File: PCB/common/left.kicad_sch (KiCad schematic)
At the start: 89 parts, among them J2 TRS

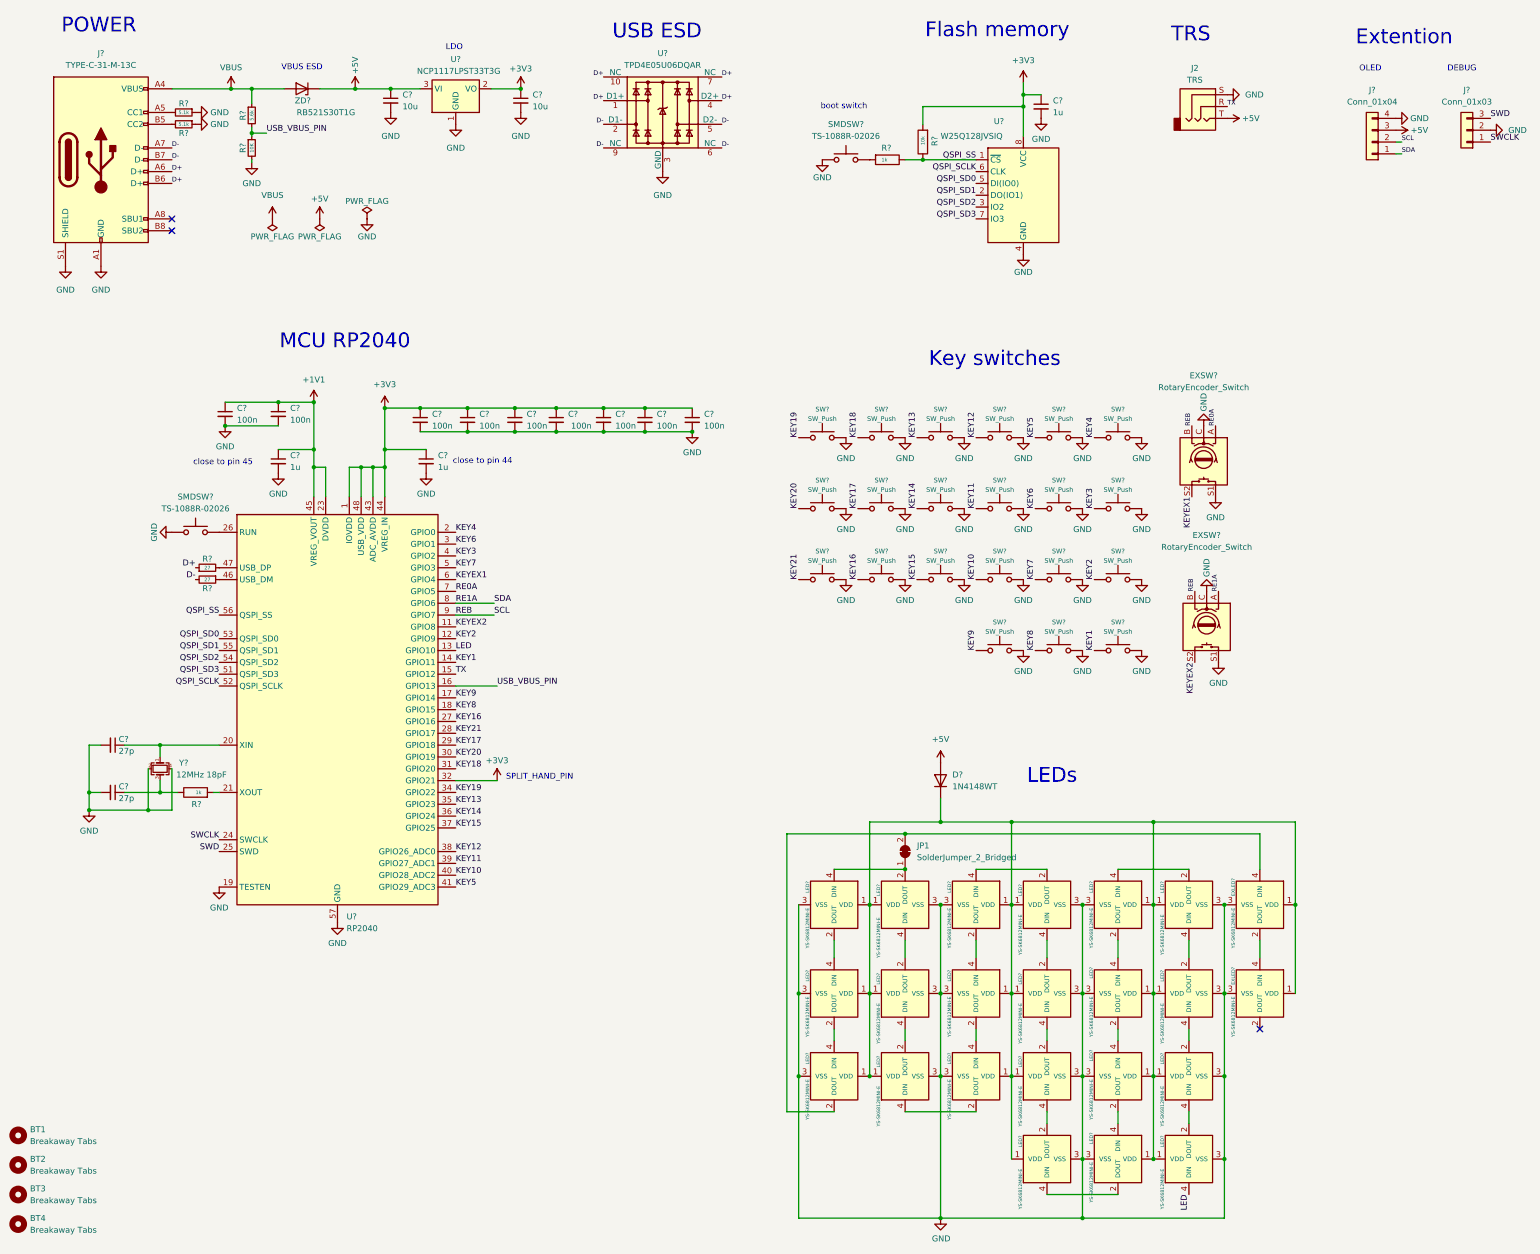
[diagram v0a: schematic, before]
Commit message: Removed unused electronics
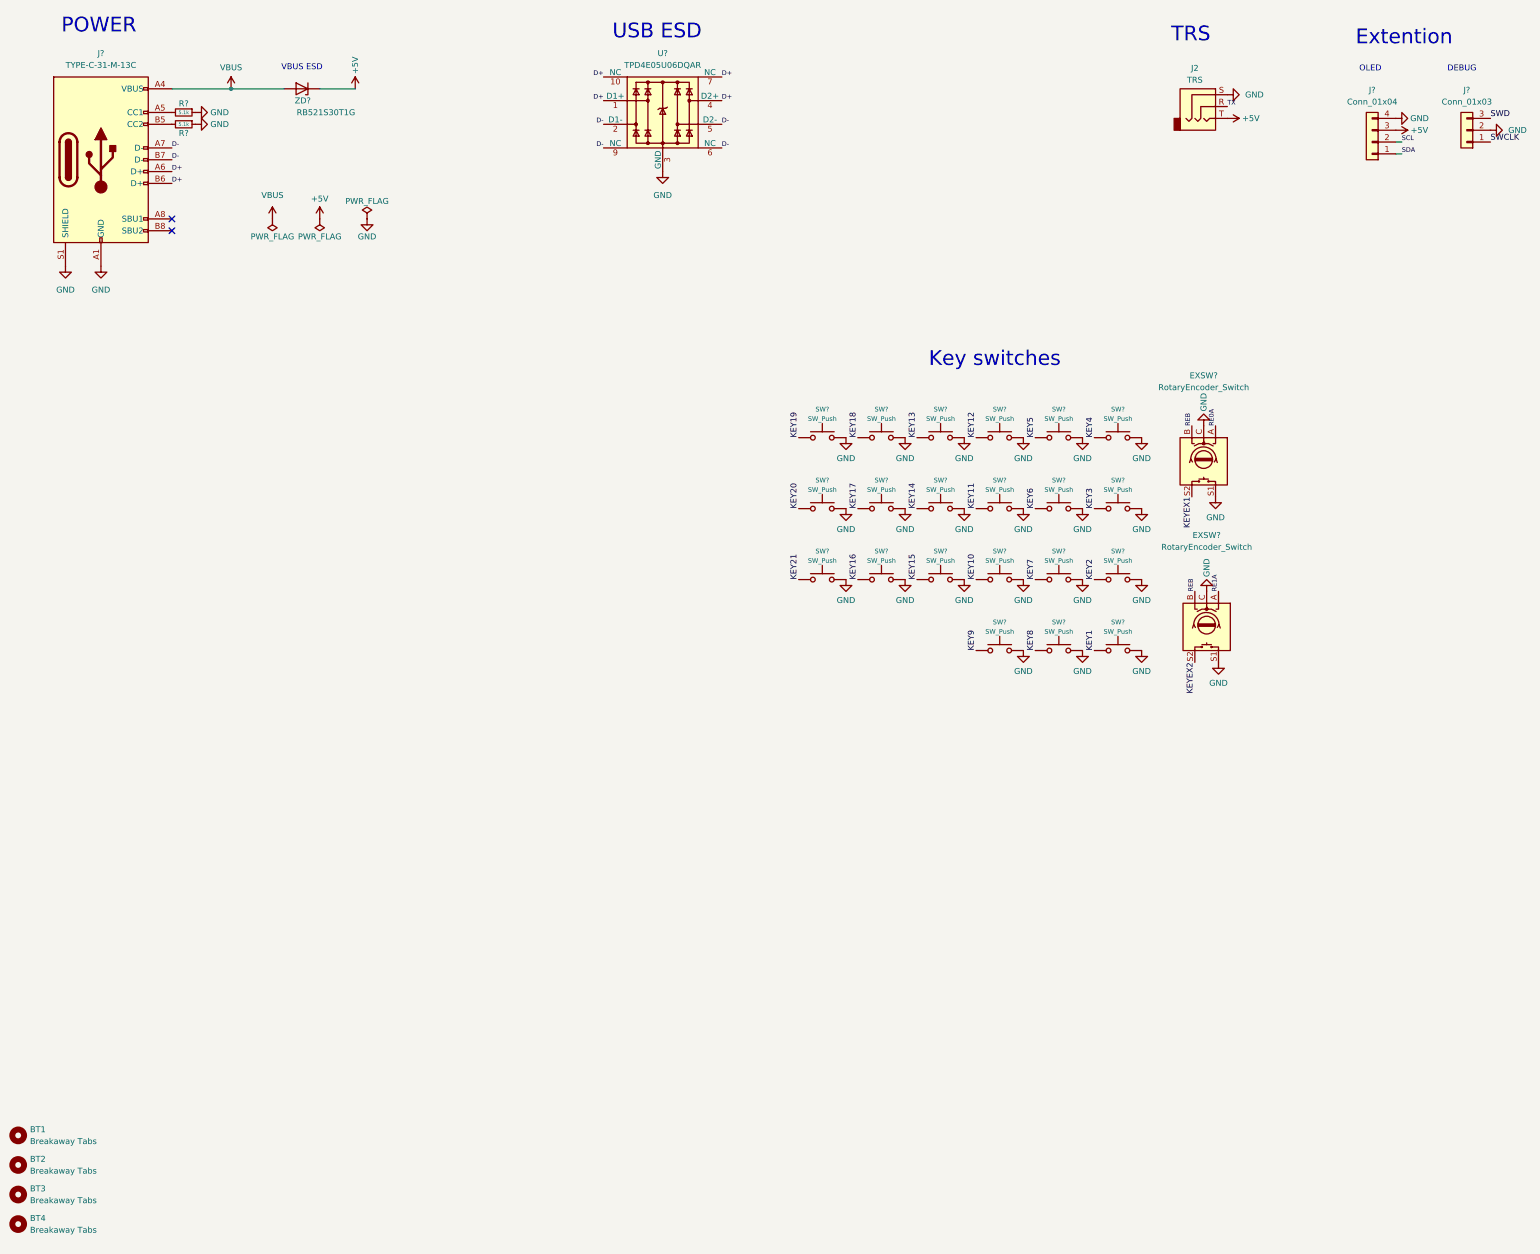
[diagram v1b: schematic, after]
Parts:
- removed C? (x2): 27p, Capacitor_SMD:C_0402_1005Metric, symbol Device:C_Small
- removed C? (x9): 100n, Capacitor_SMD:C_0402_1005Metric, symbol Device:C_Small
- removed C? (x3): 1u, Capacitor_SMD:C_0402_1005Metric, symbol Device:C_Small
- removed C? (x2): 10u, Capacitor_SMD:C_0402_1005Metric, symbol Device:C_Small
- removed D?: 1N4148WT, Diode_SMD:D_SOD-523, symbol Diode:1N4148WT
- removed EXLED? (x2), LED? (x21): YS-SK6812MINI-E, kbd_local:YS-SK6812MINI-E, symbol kbd_local:YS-SK6812MINI-E
- removed JP1: SolderJumper_2_Bridged, Jumper:SolderJumper-2_P1.3mm_Open_RoundedPad1.0x1.5mm, symbol Jumper:SolderJumper_2_Bridged
- removed R? (x2): 27, Resistor_SMD:R_0402_1005Metric, symbol Device:R_Small
- removed R?: 10K, Resistor_SMD:R_0402_1005Metric, symbol Device:R_Small
- removed R?: 5.6k, Resistor_SMD:R_0402_1005Metric, symbol Device:R_Small
- removed R?: 10k, Resistor_SMD:R_0402_1005Metric, symbol Device:R
- removed R? (x2): 1k, Resistor_SMD:R_0402_1005Metric, symbol Device:R
- removed SMDSW? (x2): TS-1088R-02026, kbd_local:TS-1088R-02026, symbol Switch:SW_Push
- removed U?: RP2040, Package_DFN_QFN:QFN-56-1EP_7x7mm_P0.4mm_EP3.2x3.2mm, symbol MCU_RaspberryPi:RP2040
- removed U?: W25Q128JVSIQ, Package_SO:SOIC-8_5.23x5.23mm_P1.27mm, symbol Memory_Flash:W25Q128JVS
- removed U?: NCP1117LPST33T3G, Package_TO_SOT_SMD:SOT-223-3_TabPin2, symbol Regulator_Linear:NCP1117-3.3_SOT223
- removed Y?: 12MHz 18pF, Crystal:Crystal_SMD_3225-4Pin_3.2x2.5mm, symbol Device:Crystal_GND24_Small
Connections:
- net RE1A: no longer J?.1 (Pin_1)
- net REB: no longer J?.2 (Pin_2)
- new net SCL: J?.2 (Pin_2)
- new net SDA: J?.1 (Pin_1)
- no-connect marks 3 -> 2
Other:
- note removed: "Flash memory"
- note removed: "LDO"
- note removed: "LEDs"
- note removed: "MCU RP2040"
- note removed: "SPLIT_HAND_PIN"
- note removed: "boot switch"
- note removed: "close to pin 44"
- note removed: "close to pin 45"
